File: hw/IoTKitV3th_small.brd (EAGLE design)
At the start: 63.2 x 58.4 mm, 13 parts

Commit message: Verdrated
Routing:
- net GND: track 0.00 -> 199.2 mm
- net +5V: track 0.00 -> 124.1 mm
- net +3V3: track 0.00 -> 93.7 mm
- net SCL: track 0.00 -> 90.0 mm
- net D13: track 0.00 -> 68.0 mm
- net SDA: track 0.00 -> 67.3 mm
- net D12: track 0.00 -> 62.9 mm
- net A3: track 0.00 -> 62.2 mm
- net D5: track 0.00 -> 49.7 mm
- net A5: track 0.00 -> 49.5 mm
- net D11: track 0.00 -> 48.3 mm
- net D2: track 0.00 -> 48.2 mm
- net D4: track 0.00 -> 47.8 mm
- net D6: track 0.00 -> 45.8 mm
- net D7: track 0.00 -> 42.5 mm, vias 0 -> 1
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
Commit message: Grove und Servo Anschluesse
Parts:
- removed HUM/TEMP: (no value), pinhead:1X03
- added I2C: 4P-2.0, Seeed-Connector:HW4-2.0
- added I2C1: I2C, Seeed-Connector:HW4-2.0
- added JP2, JP3: (no value), pinhead:2X03
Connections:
- new net A4: B1.A4, I2C.2, JP2.5
- net +5V: now also I2C.3, I2C1.3, JP2.3, JP2.4, JP3.3, JP3.4; no longer HUM/TEMP.1
- net A5: now also I2C.1, JP2.6; no longer HUM/TEMP.2
- net D8: now also JP3.6
- net D9: now also JP3.5
- net GND: now also I2C.4, I2C1.4, JP2.1, JP2.2, JP3.1, JP3.2; no longer HUM/TEMP.3
- net SCL: now also I2C1.1
- net SDA: now also I2C1.2
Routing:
- net A4: track 0.00 -> 100.2 mm
- net A5: track 49.5 -> 97.2 mm
- net D9: track 26.9 -> 62.5 mm, vias 0 -> 1
- net D8: track 10.9 -> 45.5 mm
- net GND: track 199.2 -> 231.1 mm
- net SDA: track 67.3 -> 95.7 mm
- net SCL: track 90.0 -> 71.3 mm, vias 0 -> 1
- net D13: track 68.0 -> 81.4 mm
- net D4: track 47.8 -> 37.0 mm
- net D12: track 62.9 -> 53.5 mm
- net D7: track 42.5 -> 51.7 mm, vias 1 -> 0
- net +3V3: track 93.7 -> 100.9 mm
- net TX: track 31.0 -> 24.1 mm
- net D10: track 40.3 -> 46.7 mm
- net D2: track 48.2 -> 54.1 mm
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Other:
- board text added: "A4/A5"
- board text added: "D9~ D8~ A4 A5"
- board text added: "I2C"
- board text added: "S +5 G"
- board text removed: "A5"

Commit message: R1.1
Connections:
- net A4: now also JP3.6; no longer JP2.5
- net A5: now also JP3.5; no longer JP2.6
- net D8: now also JP2.6; no longer JP3.6
- net D9: now also JP2.5; no longer JP3.5
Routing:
- net SDA: track 95.7 -> 67.0 mm, vias 0 -> 1
- net +5V: track 129.0 -> 154.5 mm
- net A3: track 56.6 -> 78.3 mm
- net A4: track 100.2 -> 85.9 mm
- net +3V3: track 100.9 -> 89.3 mm
- net D2: track 54.1 -> 44.7 mm
- net SCL: track 71.3 -> 75.2 mm, vias 1 -> 0
- net D6: track 47.1 -> 44.9 mm
- net D9: track 62.5 -> 64.6 mm, vias 1 -> 0
- net D8: track 45.5 -> 46.9 mm
- net GND: track 231.1 -> 230.1 mm
- net D11: track 53.2 -> 52.7 mm
- net D5: track 50.2 -> 49.7 mm
- net D7: vias 0 -> 1
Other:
- board text added: "A5 A4 D9~ D8~"
- board text added: "IoTKit V3 (small), Rev. 1.1, 2020 Designed to work with mbed https://github.com/mc-b/iotkitv3"
- board text added: "SS (D9) SCLK(D13) MISO(D11) MOSI(D12) +3V3 GND"
- board text removed: "D9~ D8~ A4 A5"
- board text removed: "IoTKit V3 (small), Rev. 1.0, 2020 Designed to work with mbed https://github.com/mc-b/iotkitv3"
- board text removed: "SS (D9) SCLK(D13) MOSI(D12) MISO(D11) +3V3 GND"

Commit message: V1.2 mit MEMS Temp und Proxi Sensoren
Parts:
- added PROXI: (no value), pinhead:1X04
- added TEMP: TEMP, pinhead:1X04
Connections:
- net +3V3: now also B1.3.3V, PROXI.2, TEMP.1
- net GND: now also PROXI.1, TEMP.2
- net SCL: now also PROXI.3, TEMP.3
- net SDA: now also PROXI.4, TEMP.4
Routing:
- net +3V3: track 89.3 -> 177.6 mm
- net SCL: track 75.2 -> 126.3 mm
- net SDA: track 67.0 -> 104.9 mm, vias 1 -> 0
- net A3: track 78.3 -> 56.6 mm
- net GND: track 230.1 -> 246.6 mm
- net A5: track 97.0 -> 109.4 mm
- net +5V: track 154.5 -> 162.7 mm
- net D7: track 51.7 -> 56.9 mm, vias 1 -> 0
- net A4: track 85.9 -> 81.0 mm
- net D6: track 44.9 -> 47.1 mm
- net D13: track 81.4 -> 82.6 mm
- net N$9: track 11.9 -> 11.0 mm
- net D9: track 64.6 -> 63.7 mm
- net D10: track 46.7 -> 46.0 mm
- net D8: track 46.9 -> 46.3 mm
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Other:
- board text added: "PROXI"
- board text added: "TEMP"

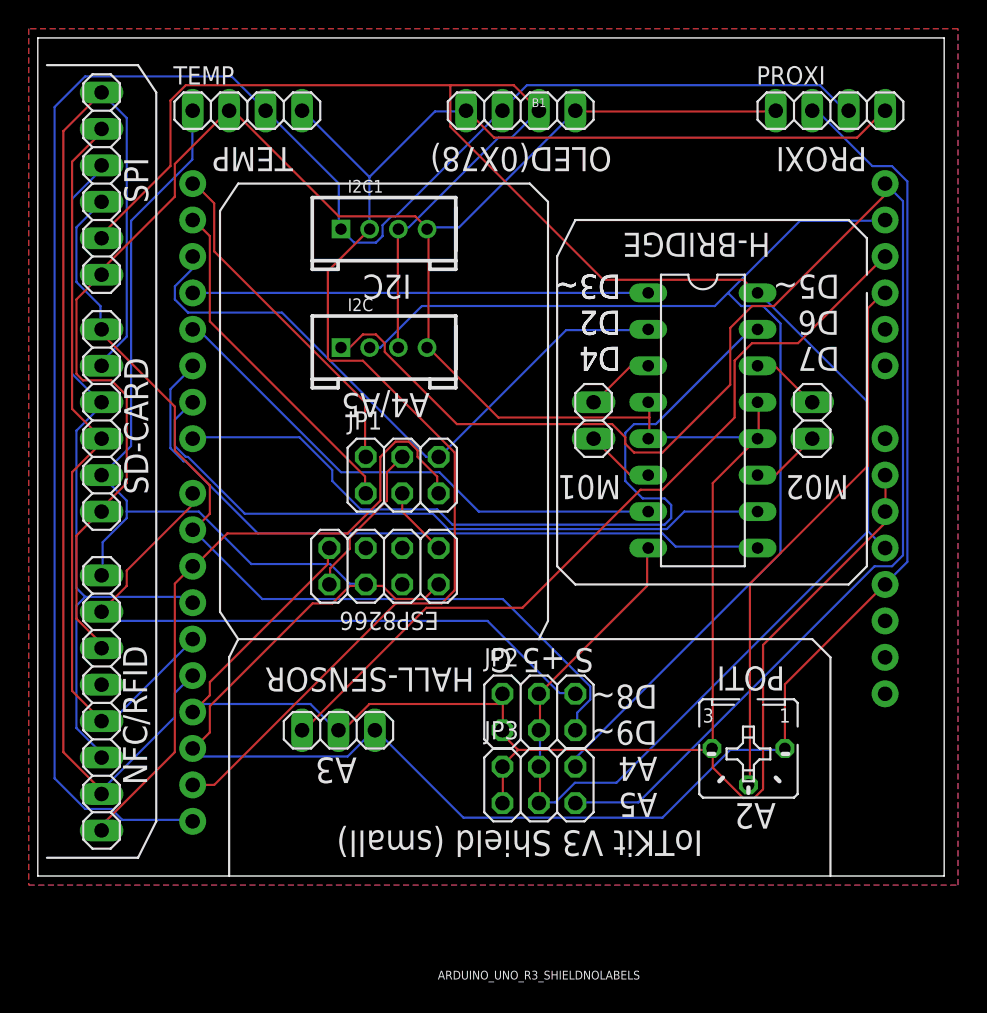
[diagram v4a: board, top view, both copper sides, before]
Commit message: Optimierungen SPI, SD Card Adapter, APDS-9960 statt 9930
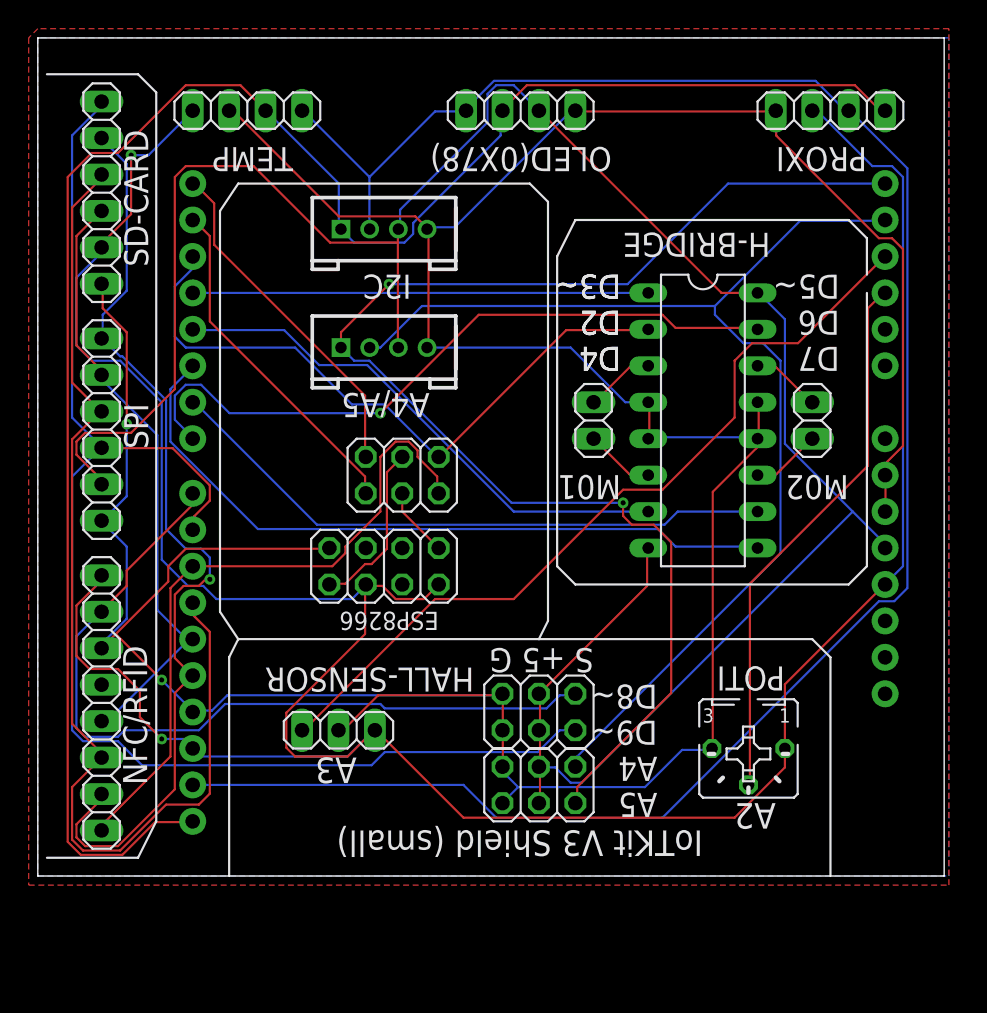
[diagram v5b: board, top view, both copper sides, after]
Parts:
- moved SPI 17.1 mm to (5.71, 32.4)
- moved SD-CARD 15.9 mm to (5.71, 48.9)
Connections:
- net SCL: now also PROXI.4; no longer PROXI.3
- net SDA: now also PROXI.3; no longer PROXI.4
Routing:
- net SDA: track 104.9 -> 139.8 mm
- net D9: track 63.7 -> 95.7 mm
- net D11: track 52.7 -> 76.1 mm
- net +3V3: track 177.6 -> 198.8 mm, vias 0 -> 2
- net D13: track 82.6 -> 66.0 mm, vias 0 -> 1
- net A5: track 109.4 -> 93.4 mm, vias 0 -> 2
- net D12: track 53.5 -> 43.0 mm
- net D8: track 46.3 -> 56.3 mm
- net D7: track 56.9 -> 48.5 mm, vias 0 -> 1
- net GND: track 246.6 -> 252.2 mm, vias 0 -> 2
- net D6: track 47.1 -> 43.3 mm
- net SCL: track 126.3 -> 129.1 mm
- net D2: track 44.7 -> 46.2 mm
- net N$9: track 11.0 -> 11.9 mm
- net D10: track 46.0 -> 46.7 mm
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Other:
- board text added: "IoTKit V3 (small), Rev. 1.2, 2021 Designed to work with mbed https://github.com/iotkitv3/intro"
- board text removed: "IoTKit V3 (small), Rev. 1.1, 2020 Designed to work with mbed https://github.com/mc-b/iotkitv3"
